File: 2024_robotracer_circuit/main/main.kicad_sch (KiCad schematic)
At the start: 126 parts, among them J1 PH_6p, J10 PH_3p, J11 PH_3p, J12 PH_4p, J14 PH_6p, J2 Conn_02x05_Odd_Even, J3 Conn_02x05_Odd_Even, J4 PA_2p, J5 PA_2p, J6 XT_2p, J7 Micro_SD_Card_Det1, J8 PH_4p, J9 PH_6p, SW1 TVGP01-G73BB, U1 STM32F405RGTx, U10 MTN2306AN3, U11 LBR-127HLD, U12 MTN2306AN3, U13 LBR-127HLD, U14 MTN2306AN3, U15 LBR-127HLD, U16 AE-BMX055, U17 MTN2306AN3, U18 MTN2306AN3, U19 LBR-127HLD, U2 OSC8MI/H, U20 MTN2306AN3, U21 LBR-127HLD, U22 SKRHAAE010, U23 SS-22F32G5, U3 AM2837, U4 AM2837, U5 BP5293-33, U6 BP5293-50, U7 SSM6J808R, U8 LBR-127HLD, U9 MTN2306AN3

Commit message: 基板わけた
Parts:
- removed D15: LED_Small, LED_SMD:LED_0603_1608Metric_Pad1.05x0.95mm_HandSolder, symbol Device:LED_Small
- removed J10, J11: PH_3p, Connector_JST:JST_PH_B3B-PH-K_1x03_P2.00mm_Vertical, symbol Connector_Generic:Conn_01x03
- removed J9: PH_6p, Connector_JST:JST_PH_B6B-PH-K_1x06_P2.00mm_Vertical, symbol Connector_Generic:Conn_01x06
- removed R18, R19, R20, R21, R25, R28: 47k, Resistor_SMD:R_0603_1608Metric_Pad0.98x0.95mm_HandSolder, symbol Device:R_Small
- removed R26, R29, R9: 4.7, Resistor_SMD:R_0603_1608Metric_Pad0.98x0.95mm_HandSolder, symbol Device:R_Small
- removed R4: 1k, Resistor_SMD:R_0603_1608Metric_Pad0.98x0.95mm_HandSolder, symbol Device:R_Small
- removed R46: R_Small, Resistor_SMD:R_0603_1608Metric_Pad0.98x0.95mm_HandSolder, symbol Device:R_Small
- removed U11, U13, U15, U19, U21, U8: LBR-127HLD, mylib:LBR-127HLD, symbol mylib:LBR-127HLD
- removed U12, U14, U18, U20, U9: MTN2306AN3, Package_TO_SOT_SMD:SOT-23, symbol mylib:MTN2306AN3
- added J10, J9: PH_5p, Connector_JST:JST_PH_B5B-PH-K_1x05_P2.00mm_Vertical, symbol Connector_Generic:Conn_01x05
- added J13: PH_8p, Connector_JST:JST_PH_B8B-PH-K_1x08_P2.00mm_Vertical, symbol Connector_Generic:Conn_01x08
- added U8: MTN2306AN3, Package_TO_SOT_SMD:TSOT-23, symbol mylib:MTN2306AN3
- R2: value R -> 47k
- R3, R7: value 4.7 -> 47k
- R5: value 4.7 -> 1k
- U10: footprint Package_TO_SOT_SMD:SOT-23 -> Package_TO_SOT_SMD:TSOT-23
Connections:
- net LED10 is gone; now on net LED9: U1.45 (PA12)
- net SENSOR1_PWM is gone; now on net SENSOR_PWM: U10.1 (G)
- net +3.3V: now also R36.1, R37.1, R38.1, R39.1, R5.1, R6.1, J10.1 (Pin_1), J13.1 (Pin_1), J9.1 (Pin_1)
- net +5V: now also J10.2 (Pin_2), J13.2 (Pin_2), J9.2 (Pin_2); no longer R36.1, R37.1, R38.1, R39.1, R6.1
- net GND: now also R3.2, R7.2, U10.2 (S), U17.2 (S), J10.5 (Pin_5), J13.8 (Pin_8), J9.5 (Pin_5), U8.2 (S); no longer U10.3 (S), U17.3 (S)
- net LED2: now also U1.2 (PC13); no longer U1.40 (PC9)
- net LED3: now also U1.3 (PC14); no longer U1.2 (PC13)
- net LED4: now also U1.4 (PC15); no longer U1.3 (PC14)
- net LED5: now also U1.33 (PB12); no longer U1.4 (PC15)
- net LED6: now also U1.57 (PB5); no longer U1.33 (PB12)
- net LED7: now also U1.56 (PB4); no longer U1.57 (PB5)
- net LED8: now also U1.28 (PB2); no longer U1.56 (PB4)
- net LED9: no longer U1.28 (PB2)
- net SENSOR0_ADC: now also J13.3 (Pin_3)
- net SENSOR1_ADC: now also J13.4 (Pin_4)
- net SENSOR2_ADC: now also J13.5 (Pin_5)
- net SENSOR3_ADC: now also J13.6 (Pin_6)
- net SENSOR_L_ADC: now also R5.2, J10.3 (Pin_3)
- net SENSOR_R_ADC: now also J9.3 (Pin_3)
- net SENSOR_PWM: now reaches R3.1
- net SENSOR_PWM: now also R7.1, U1.40 (PC9), U8.1 (G)
- net at BZ1.2 (-), D1.2 (A): now also U17.3 (D); no longer U17.2 (D)
- new net: J10.4 (Pin_4), J9.4 (Pin_4), U10.3 (D)
- new net: J13.7 (Pin_7), U8.3 (D)
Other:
- moved on the sheet: C11, C12, C13, C14, C24, C25, D10, D11, D12, D13, D14, D5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

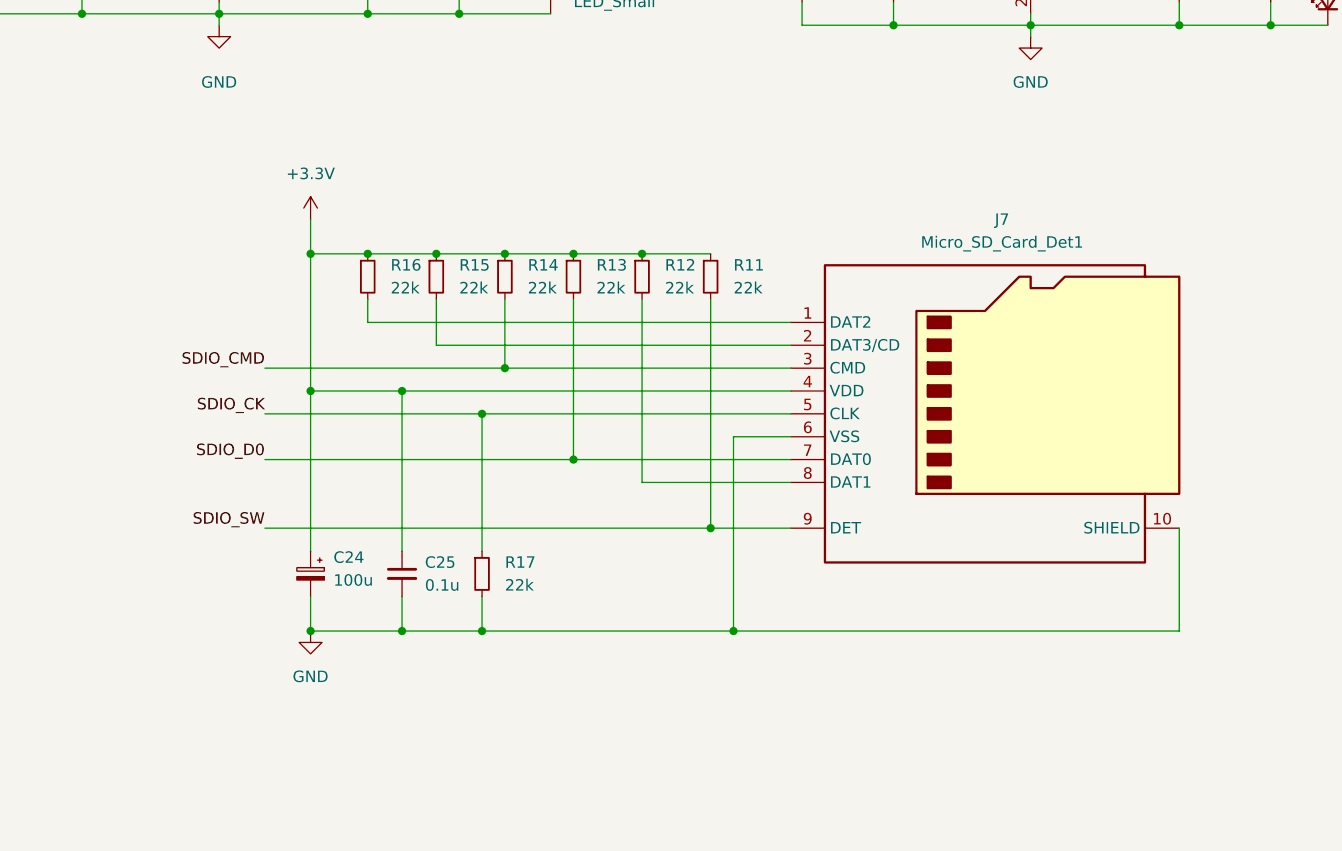
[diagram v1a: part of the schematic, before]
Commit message: SDカード分けた
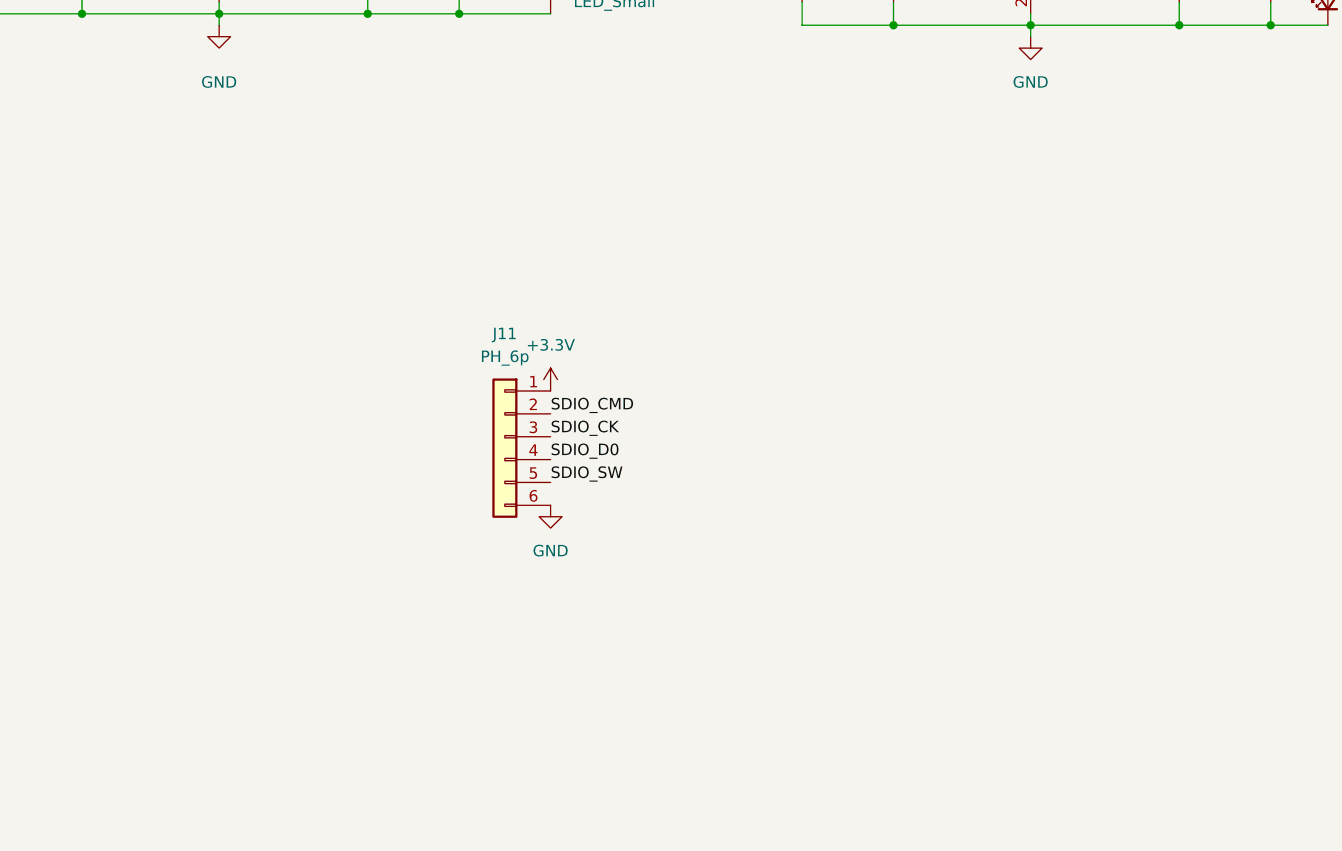
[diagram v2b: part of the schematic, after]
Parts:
- removed C24: 100u, Capacitor_SMD:CP_Elec_6.3x5.4, symbol Device:C_Polarized_Small
- removed C25: 0.1u, Capacitor_SMD:C_0603_1608Metric_Pad1.08x0.95mm_HandSolder, symbol Device:C_Small
- removed J7: Micro_SD_Card_Det1, Connector_Card:microSD_HC_Hirose_DM3AT-SF-PEJM5, symbol Connector:Micro_SD_Card_Det1
- removed R11, R12, R13, R14, R15, R16, R17: 22k, Resistor_SMD:R_0603_1608Metric_Pad0.98x0.95mm_HandSolder, symbol Device:R_Small
- added J11: PH_6p, Connector_JST:JST_PH_B6B-PH-K_1x06_P2.00mm_Vertical, symbol Connector_Generic:Conn_01x06
- J6: footprint Connector_AMASS:AMASS_XT30U-M_1x02_P5.0mm_Vertical -> Connector_AMASS:AMASS_XT30PW-M_1x02_P2.50mm_Horizontal
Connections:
- net +3.3V: now also J11.1 (Pin_1)
- net GND: now also J11.6 (Pin_6)
- net SDIO_CK: now also J11.3 (Pin_3)
- net SDIO_CMD: now also J11.2 (Pin_2)
- net SDIO_D0: now also J11.4 (Pin_4)
- net SDIO_SW: now also J11.5 (Pin_5)

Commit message: パターン引き中
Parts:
- removed C17, C22: 100u, Capacitor_SMD:CP_Elec_6.3x5.4, symbol Device:C_Polarized_Small
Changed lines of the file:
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@@
 	)
 	(junction
-		(at 166.37 48.26)
-		(diameter 0)
-		(color 0 0 0 0)
-	)
-	(junction
 		(at 256.54 39.37)
 		(diameter 0)
@@
 	)
 	(junction
-		(at 256.54 49.53)
-		(diameter 0)
-		(color 0 0 0 0)
-	)
-	(junction
 		(at 187.96 199.39)
 		(diameter 0)
@@
 	(wire
 		(pts
-			(xy 156.21 48.26) (xy 166.37 48.26)
+			(xy 156.21 48.26) (xy 176.53 48.26)
 		)
 		(stroke
@@
 	(wire
 		(pts
-			(xy 166.37 45.72) (xy 166.37 48.26)
-		)
-		(stroke
-			(width 0)
-			(type default)
-		)
-	)
-	(wire
-		(pts
 			(xy 330.2 38.1) (xy 339.09 38.1)
 		)
@@
 	(wire
 		(pts
-			(xy 256.54 46.99) (xy 256.54 49.53)
-		)
-		(stroke
-			(width 0)
-			(type default)
-		)
-	)
-	(wire
-		(pts
 			(xy 213.36 217.17) (xy 227.33 217.17)
 		)
@@
 	(wire
 		(pts
-			(xy 166.37 48.26) (xy 176.53 48.26)
-		)
-		(stroke
-			(width 0)
-			(type default)
-		)
-	)
-	(wire
-		(pts
 			(xy 369.57 220.98) (xy 364.49 220.98)
 		)
@@
 	(wire
 		(pts
-			(xy 256.54 49.53) (xy 262.89 49.53)
+			(xy 246.38 49.53) (xy 262.89 49.53)
 		)
 		(stroke
@@
 	(wire
 		(pts
-			(xy 256.54 39.37) (xy 256.54 41.91)
-		)
-		(stroke
-			(width 0)
-			(type default)
-		)
-	)
-	(wire
-		(pts
 			(xy 330.2 215.9) (xy 330.2 227.33)
 		)
@@
 	(wire
 		(pts
-			(xy 246.38 49.53) (xy 256.54 49.53)
-		)
-		(stroke
-			(width 0)
-			(type default)
-		)
-	)
-	(wire
-		(pts
 			(xy 293.37 35.56) (xy 283.21 35.56)
 		)
@@
 	(wire
 		(pts
-			(xy 166.37 38.1) (xy 166.37 40.64)
-		)
-		(stroke
-			(width 0)
-			(type default)
-		)
-	)
-	(wire
-		(pts
 			(xy 27.94 83.82) (xy 27.94 90.17)
 		)
@@
 	)
 	(symbol
-		(lib_id "Device:C_Polarized_Small")
-		(at 256.54 44.45 0)
-		(mirror y)
-		(unit 1)
-		(exclude_from_sim no)
-		(in_bom yes)
-		(on_board yes)
-		(dnp no)
-		(fields_autoplaced yes)
-		(property "Reference" "C22"
-			(at 254 42.6338 0)
-			(effects
-				(font
-					(size 1.27 1.27)
-				)
-				(justify left)
-			)
-		)
-		(property "Value" "100u"
-			(at 254 45.1738 0)
-			(effects
-				(font
-					(size 1.27 1.27)
-				)
-				(justify left)
-			)
-		)
-		(property "Footprint" "Capacitor_SMD:CP_Elec_6.3x5.4"
-			(at 256.54 44.45 0)
-			(effects
-				(font
-					(size 1.27 1.27)
-				)
-				(hide yes)
-			)
-		)
-		(property "Datasheet" "~"
-			(at 256.54 44.45 0)
-			(effects
-				(font
-					(size 1.27 1.27)
-				)
-				(hide yes)
-			)
-		)
-		(property "Description" "Polarized capacitor, small symbol"
-			(at 256.54 44.45 0)
-			(effects
-				(font
-					(size 1.27 1.27)
-				)
-				(hide yes)
-			)
-		)
-		(pin "2"
-		)
-		(pin "1"
-		)
-		(instances
-			(project "main"
-				(path "/17779a84-a458-4dfa-8c72-c0044fe3feb5"
-					(reference "C22")
-					(unit 1)
-				)
-			)
-		)
-	)
-	(symbol
 		(lib_id "Device:LED_Small")
 		(at 88.9 153.67 90)
@@
 					(unit 1)
 				)
-			)
-		)
-	)
-	(symbol
-		(lib_id "Device:C_Polarized_Small")
-		(at 166.37 43.18 0)
-		(mirror y)
-		(unit 1)
-		(exclude_from_sim no)
-		(in_bom yes)
-		(on_board yes)
-		(dnp no)
-		(fields_autoplaced yes)
-		(property "Reference" "C17"
-			(at 163.83 41.3638 0)
-			(effects
-				(font
-					(size 1.27 1.27)
-				)
-				(justify left)
-			)
-		)
-		(property "Value" "100u"
-			(at 163.83 43.9038 0)
-			(effects
-				(font
-					(size 1.27 1.27)
-				)
-				(justify left)
-			)
-		)
-		(property "Footprint" "Capacitor_SMD:CP_Elec_6.3x5.4"
-			(at 166.37 43.18 0)
-			(effects
-				(font
-					(size 1.27 1.27)
-				)
-				(hide yes)
-			)
-		)
-		(property "Datasheet" "~"
-			(at 166.37 43.18 0)
-			(effects
-				(font
-					(size 1.27 1.27)
-				)
-				(hide yes)
-			)
-		)
-		(property "Description" "Polarized capacitor, small symbol"
-			(at 166.37 43.18 0)
-			(effects
-				(font
-					(size 1.27 1.27)
-				)
-				(hide yes)
-			)
-		)
-		(pin "2"
-		)
-		(pin "1"
-		)
-		(instances
-			(project "main"
-				(path "/17779a84-a458-4dfa-8c72-c0044fe3feb5"
-					(reference "C17")
-					(unit 1)
-				)

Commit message: とちゅう
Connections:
- net at U3.7 (OUT_A), U3.8 (OUT_A): now also J4.2 (Pin_2); no longer J4.1 (Pin_1)
- net at U3.5 (OUT_B), U3.6 (OUT_B): now also J4.1 (Pin_1); no longer J4.2 (Pin_2)
- net at U4.5 (OUT_B), U4.6 (OUT_B): now also J5.1 (Pin_1); no longer J5.2 (Pin_2)
- net at U4.7 (OUT_A), U4.8 (OUT_A): now also J5.2 (Pin_2); no longer J5.1 (Pin_1)
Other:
- moved on the sheet: C1, C10, C19, C2, C20, C21, C3, C4, C5, C6, C7, C8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

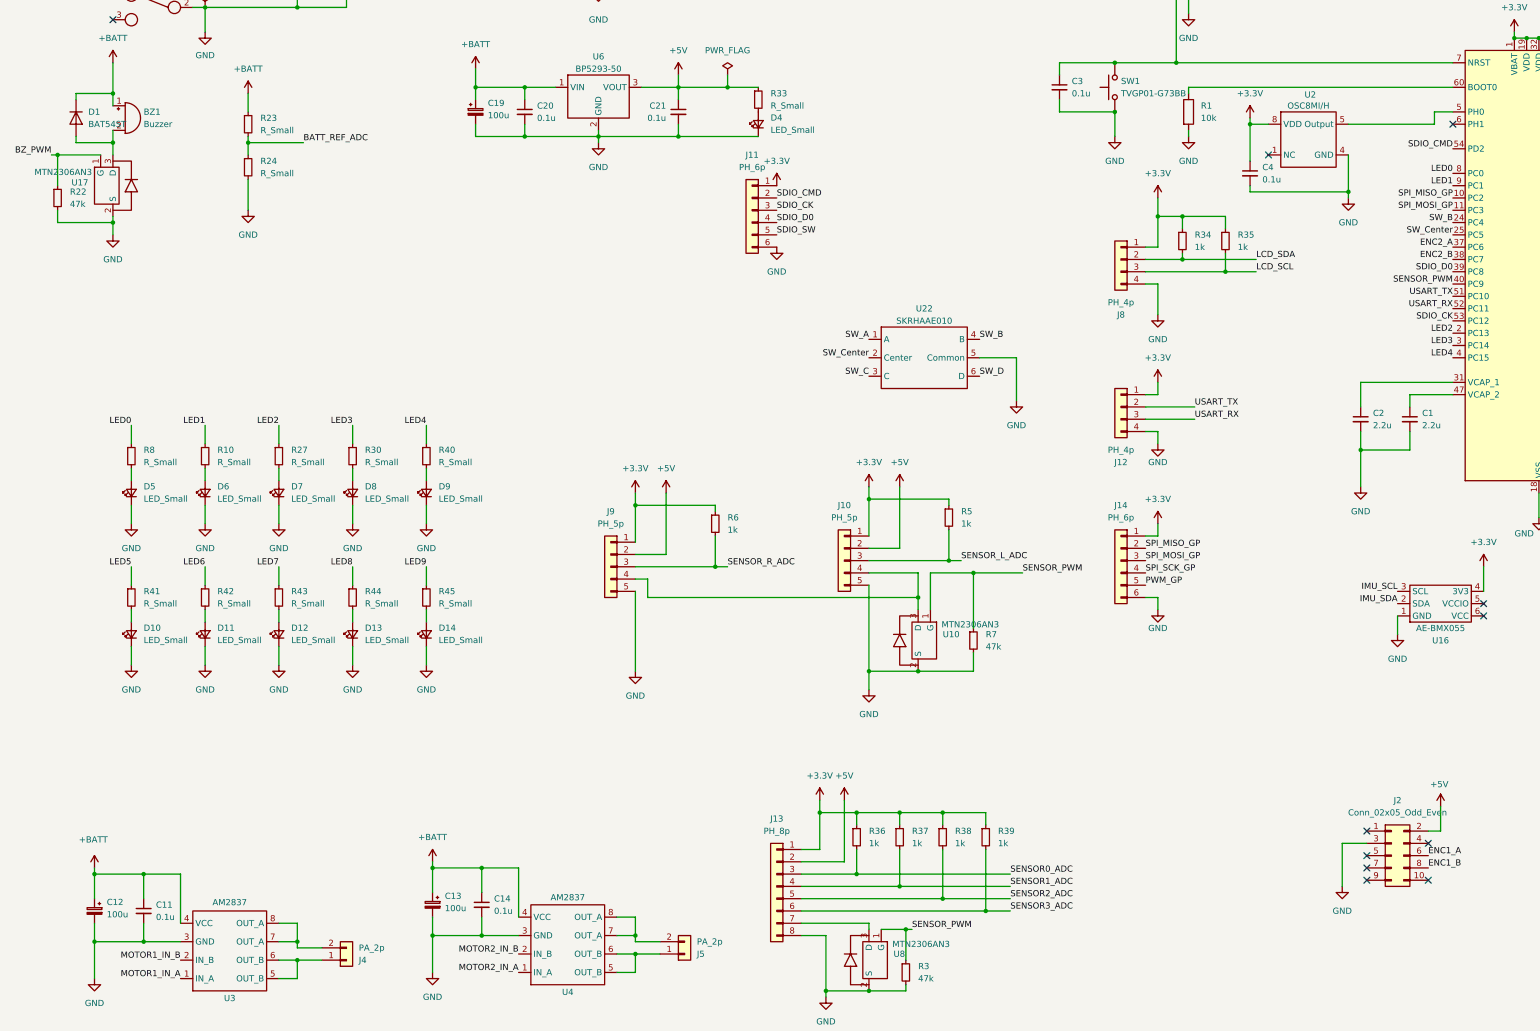
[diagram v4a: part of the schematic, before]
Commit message: LED基板分けた
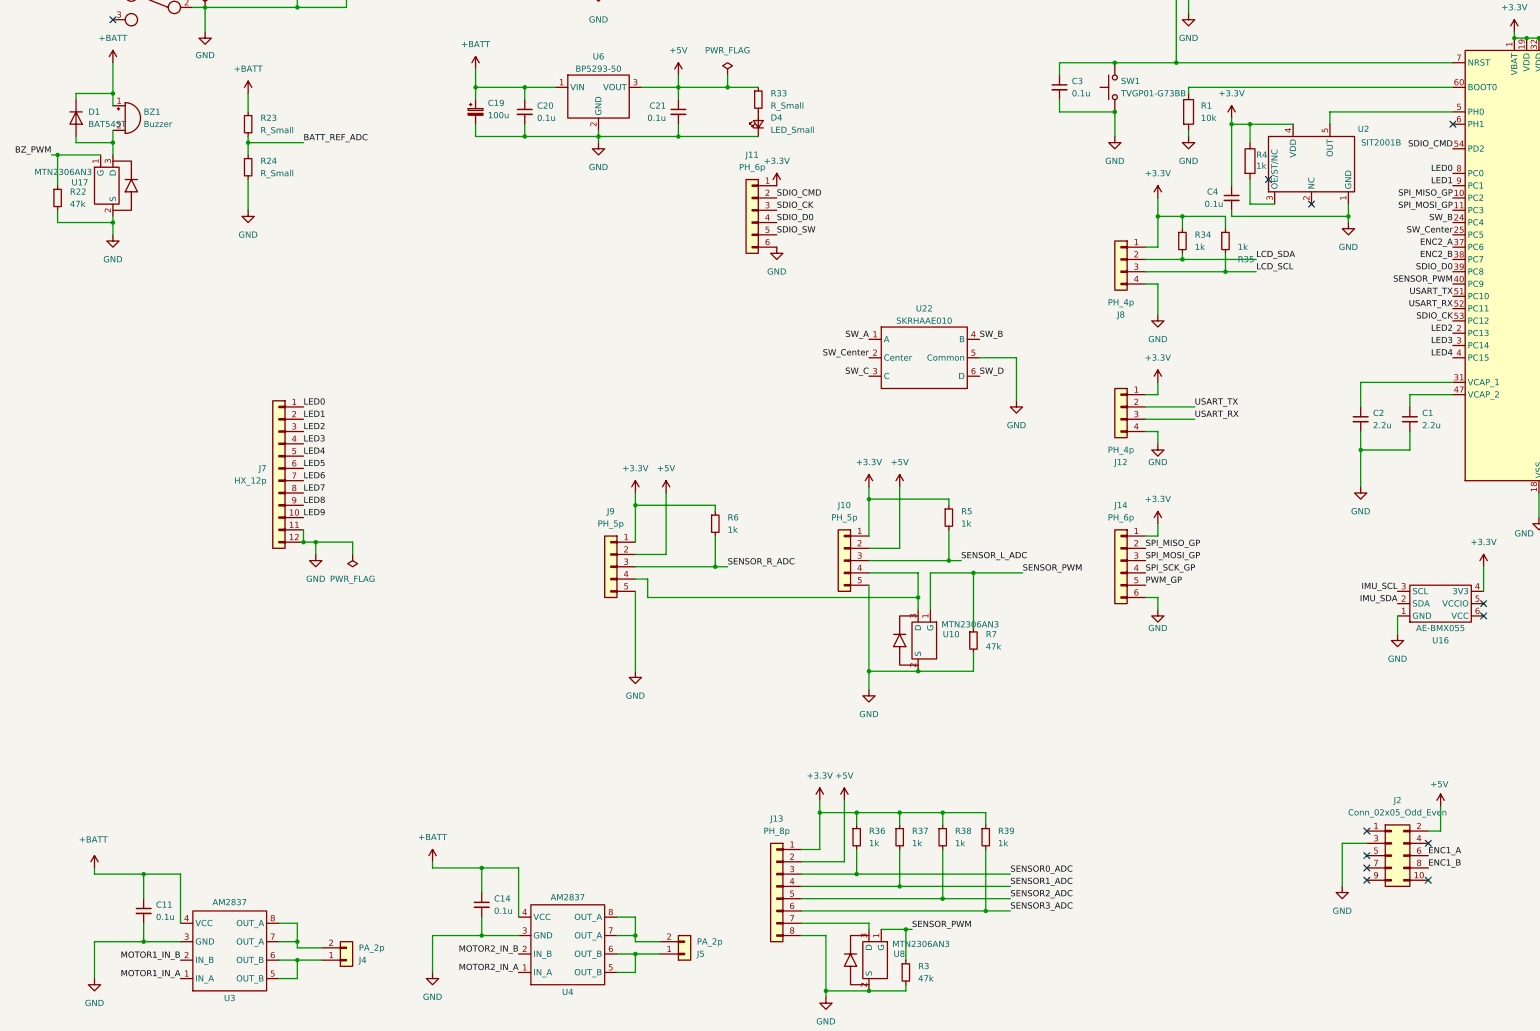
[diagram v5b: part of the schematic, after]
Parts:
- removed C12, C13: 100u, Capacitor_SMD:CP_Elec_6.3x5.4, symbol Device:C_Polarized_Small
- removed D10, D11, D12, D13, D14, D5, D6, D7, D8, D9: LED_Small, LED_SMD:LED_0603_1608Metric_Pad1.05x0.95mm_HandSolder, symbol Device:LED_Small
- removed R10, R27, R30, R40, R41, R42, R43, R44, R45, R8: R_Small, Resistor_SMD:R_0603_1608Metric_Pad0.98x0.95mm_HandSolder, symbol Device:R_Small
- removed U2: OSC8MI/H, mylib:OSC8MIH, symbol mylib:OSC
- added J7: HX_12p, Connector_JST:JST_XH_B12B-XH-A_1x12_P2.50mm_Vertical, symbol Connector_Generic:Conn_01x12
- added R4: 1k, Resistor_SMD:R_0603_1608Metric_Pad0.98x0.95mm_HandSolder, symbol Device:R
- added U2: SIT2001B, Package_TO_SOT_SMD:TSOT-23-5, symbol mylib:SIT2001B
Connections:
- net +3.3V: now also R4.1, U2.4 (VDD)
- net GND: now also J7.11 (Pin_11), J7.12 (Pin_12), U2.1 (GND)
- net LED0: now also J7.1 (Pin_1)
- net LED1: now also J7.2 (Pin_2)
- net LED2: now also J7.3 (Pin_3)
- net LED3: now also J7.4 (Pin_4)
- net LED4: now also J7.5 (Pin_5)
- net LED5: now also J7.6 (Pin_6)
- net LED6: now also J7.7 (Pin_7)
- net LED7: now also J7.8 (Pin_8)
- net LED8: now also J7.9 (Pin_9)
- net LED9: now also J7.10 (Pin_10)
- net at U1.5 (PH0): now also U2.5 (OUT)
- new net: R4.2, U2.3 (OE/ST/NC)
- no-connect marks 17 -> 18
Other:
- moved on the sheet: C4

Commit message: 配線途中
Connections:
- net ENC2_A: now also U1.38 (PC7); no longer U1.37 (PC6)
- net ENC2_B: now also U1.37 (PC6); no longer U1.38 (PC7)
- net LCD_SCL: now also J8.2 (Pin_2), R34.2; no longer J8.3 (Pin_3), R35.2
- net LCD_SDA: now also J8.3 (Pin_3), R35.2; no longer J8.2 (Pin_2), R34.2
- net SDIO_CK: now also J11.4 (Pin_4); no longer J11.3 (Pin_3)
- net SDIO_CMD: now also J11.5 (Pin_5); no longer J11.2 (Pin_2)
- net SDIO_D0: now also J11.2 (Pin_2); no longer J11.4 (Pin_4)
- net SDIO_SW: now also J11.3 (Pin_3); no longer J11.5 (Pin_5)
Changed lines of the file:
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@@
 	)
 	(label "SDIO_CMD"
-		(at 176.53 92.71 0)
+		(at 176.53 100.33 0)
 		(fields_autoplaced yes)
 		(effects
@@
 	)
 	(label "SDIO_D0"
-		(at 176.53 97.79 0)
+		(at 176.53 92.71 0)
 		(fields_autoplaced yes)
 		(effects
@@
 	)
 	(label "LCD_SCL"
-		(at 275.59 107.95 0)
+		(at 275.59 105.41 0)
 		(fields_autoplaced yes)
 		(effects
@@
 	)
 	(label "ENC2_A"
-		(at 316.23 102.87 180)
+		(at 316.23 105.41 180)
 		(fields_autoplaced yes)
 		(effects
@@
 	)
 	(label "LCD_SDA"
-		(at 275.59 105.41 0)
+		(at 275.59 107.95 0)
 		(fields_autoplaced yes)
 		(effects
@@
 	)
 	(label "ENC2_B"
-		(at 316.23 105.41 180)
+		(at 316.23 102.87 180)
 		(fields_autoplaced yes)
 		(effects
@@
 	)
 	(label "SDIO_SW"
-		(at 176.53 100.33 0)
+		(at 176.53 95.25 0)
 		(fields_autoplaced yes)
 		(effects
@@
 	)
 	(label "SDIO_CK"
-		(at 176.53 95.25 0)
-		(fields_autoplaced yes)
-		(effects
+		(at 176.53 97.79 0)
+		(fields_autoplaced yes)
+		(effects

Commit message: マイコン向き変えたい
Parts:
- removed C10: 0.1u, Capacitor_SMD:C_0603_1608Metric_Pad1.08x0.95mm_HandSolder, symbol Device:C_Small
- removed FB1, FB2: FerriteBead_Small, Resistor_SMD:R_0603_1608Metric_Pad0.98x0.95mm_HandSolder, symbol Device:FerriteBead_Small
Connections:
- net GNDA is gone; now on net GND: U1.12 (VSSA)
- net VDDA is gone; now on net +3.3V: U1.13 (VDDA)
- net USART_RX: now also J12.2 (Pin_2); no longer J12.3 (Pin_3)
- net USART_TX: now also J12.3 (Pin_3); no longer J12.2 (Pin_2)
